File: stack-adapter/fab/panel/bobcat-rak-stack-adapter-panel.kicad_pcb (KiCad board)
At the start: 2 copper layers, 78.6 x 60.3 mm, 80 parts, among them J1_0 PCIE-52P52H, J1_1 PCIE-52P52H

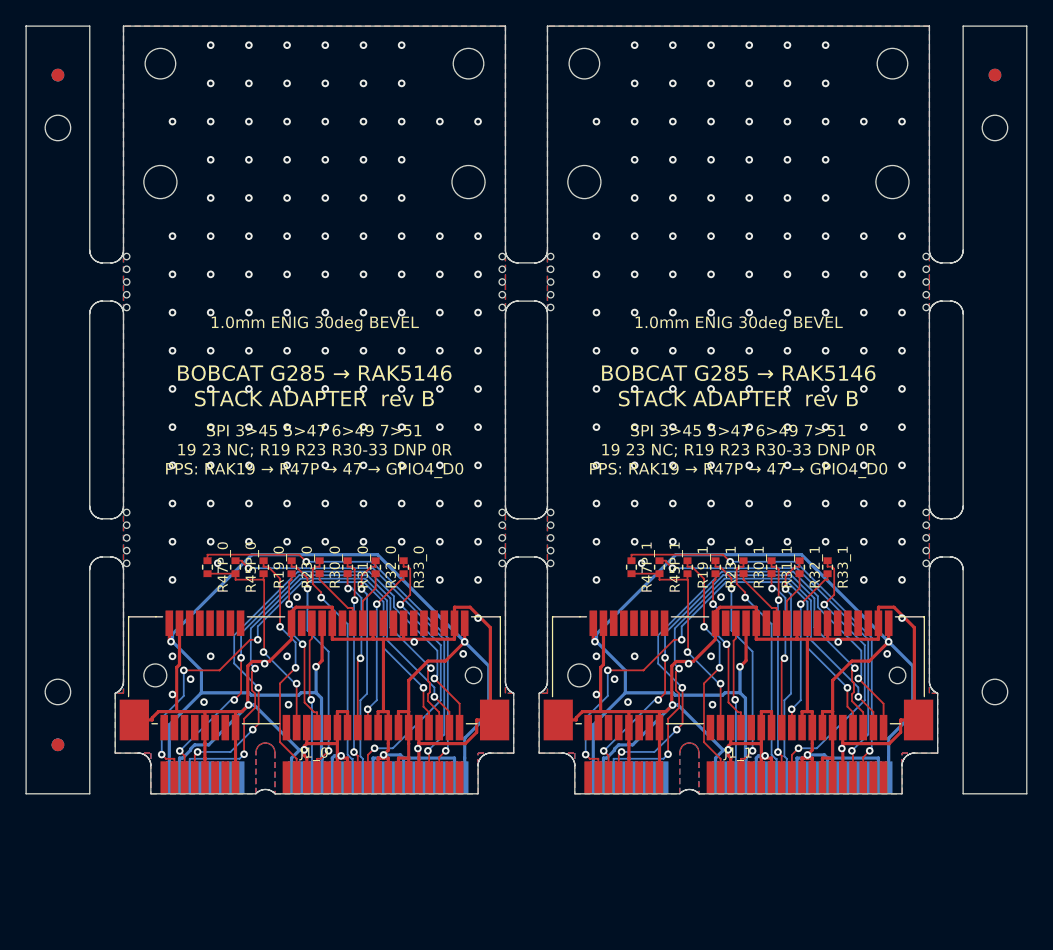
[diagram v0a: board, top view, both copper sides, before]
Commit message: stack-adapter: 70.5 mm panel (top-only rail) for JLC Standard PCBA; order notes
Standard PCBA (forced by ENIG/gold fingers) needs >= 70 x 70 mm, and JLC-added rails would cover the
finger edge, so the panel gets an 8 mm top rail only: 78.6 x 70.5 mm, fingers flush and bare on the
bottom. DRC clean; gerber_check passes. README order section updated (Standard top, no remark).

Co-Authored-By: Claude Opus 5.5 <noreply@anthropic.com>
Claude-Session: https://claude.ai/code/session_01Au7yLXRzrrweJwAkfxbhgS
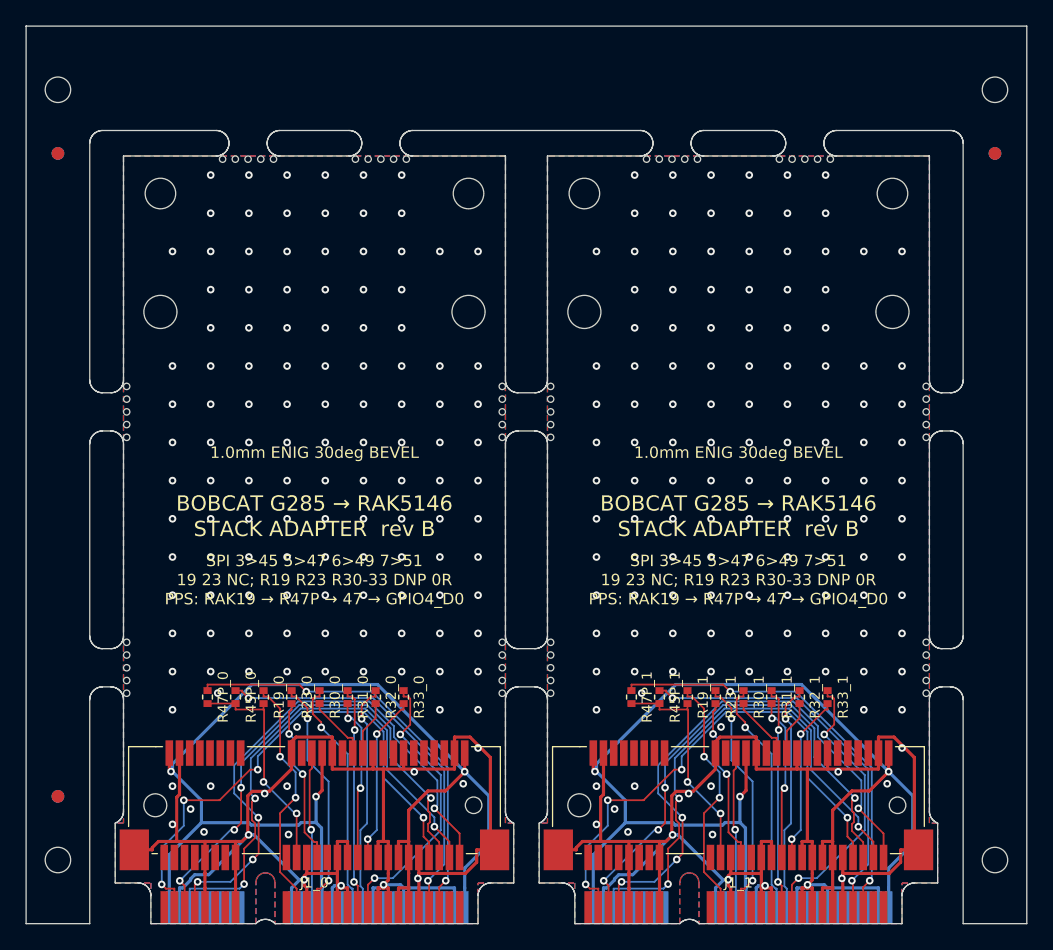
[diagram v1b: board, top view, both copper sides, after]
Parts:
- added KiKit_MB_10_1: NPTH, NPTH, F.Cu at (179.9, 68.4)
- added KiKit_MB_10_2: NPTH, NPTH, F.Cu at (179.9, 69.4)
- added KiKit_MB_10_3: NPTH, NPTH, F.Cu at (179.9, 70.4)
- added KiKit_MB_10_4: NPTH, NPTH, F.Cu at (179.9, 71.4)
- added KiKit_MB_10_5: NPTH, NPTH, F.Cu at (179.9, 72.4)
- added KiKit_MB_11_1: NPTH, NPTH, F.Cu at (157.9, 30.4)
- added KiKit_MB_11_2: NPTH, NPTH, F.Cu at (158.9, 30.4)
- added KiKit_MB_11_3: NPTH, NPTH, F.Cu at (159.9, 30.4)
- added KiKit_MB_11_4: NPTH, NPTH, F.Cu at (160.9, 30.4)
- added KiKit_MB_11_5: NPTH, NPTH, F.Cu at (161.9, 30.4)
- added KiKit_MB_12_1: NPTH, NPTH, F.Cu at (168.4, 30.4)
- added KiKit_MB_12_2: NPTH, NPTH, F.Cu at (169.4, 30.4)
- added KiKit_MB_12_3: NPTH, NPTH, F.Cu at (170.4, 30.4)
- added KiKit_MB_12_4: NPTH, NPTH, F.Cu at (171.4, 30.4)
- added KiKit_MB_12_5: NPTH, NPTH, F.Cu at (172.4, 30.4)
- added KiKit_MB_9_1: NPTH, NPTH, F.Cu at (179.9, 48.3)
- added KiKit_MB_9_2: NPTH, NPTH, F.Cu at (179.9, 49.3)
- added KiKit_MB_9_3: NPTH, NPTH, F.Cu at (179.9, 50.3)
- added KiKit_MB_9_4: NPTH, NPTH, F.Cu at (179.9, 51.3)
- added KiKit_MB_9_5: NPTH, NPTH, F.Cu at (179.9, 52.3)
- moved KiKit_MB_6_1 35.3 mm to (135.1, 30.4)
- moved KiKit_MB_6_2 33.9 mm to (136.1, 30.4)
- moved KiKit_MB_8_1 32.7 mm to (150.4, 72.4)
- moved KiKit_MB_7_1 32.7 mm to (150.4, 52.3)
- moved KiKit_MB_6_3 32.6 mm to (137.1, 30.4)
- moved KiKit_MB_7_2 31.9 mm to (150.4, 51.3)
- moved KiKit_MB_8_2 31.9 mm to (150.4, 71.4)
- moved KiKit_MB_6_4 31.3 mm to (138.1, 30.4)
- moved KiKit_MB_8_3 31.2 mm to (150.4, 70.4)
- moved KiKit_MB_7_3 31.2 mm to (150.4, 50.3)
- moved KiKit_MB_7_4 30.6 mm to (150.4, 49.3)
- moved KiKit_MB_8_4 30.6 mm to (150.4, 69.4)
- moved KiKit_MB_7_5 30.1 mm to (150.4, 48.3)
- moved KiKit_MB_8_5 30.1 mm to (150.4, 68.4)
- moved KiKit_MB_6_5 30.0 mm to (139.1, 30.4)
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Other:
- board size 78.6 x 60.3 mm -> 78.6 x 70.5 mm
